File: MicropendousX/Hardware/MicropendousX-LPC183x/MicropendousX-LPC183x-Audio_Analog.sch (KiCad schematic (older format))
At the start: 9 parts, among them IC1 LPC183X, J1 DC_POWER_JACK, U9 OPENNECT-CONTROLLER-I2S_3V3-P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

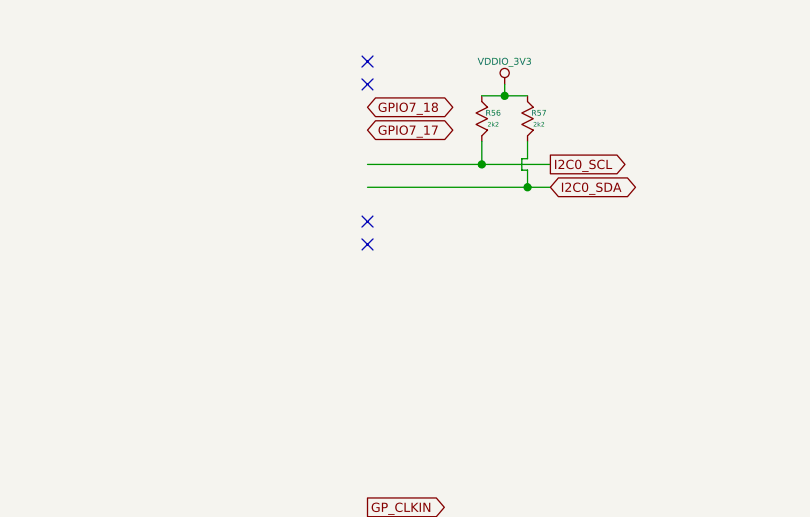
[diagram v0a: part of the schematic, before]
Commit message: Update unfinished LPC183x-based design.
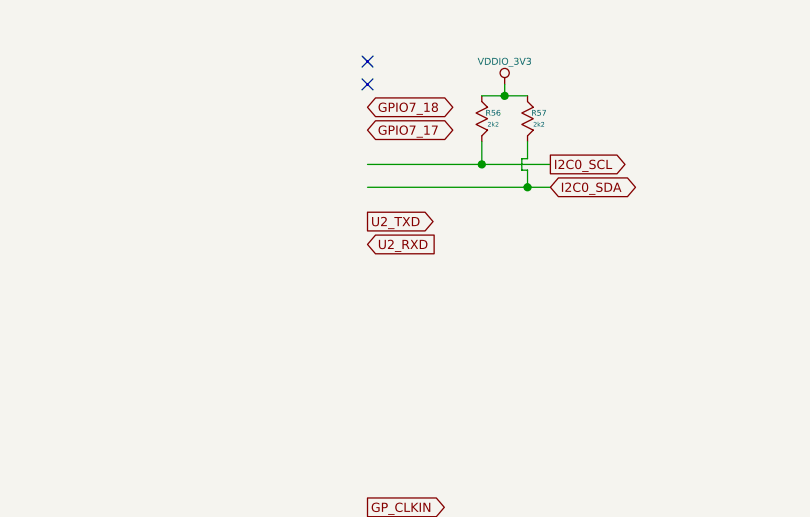
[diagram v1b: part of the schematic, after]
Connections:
- net labels added: U2_RXD, U2_TXD
- no-connect marks 18 -> 16
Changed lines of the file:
@@
-EESchema Schematic File Version 2  date 8/15/2011 4:26:38 PM
+EESchema Schematic File Version 2  date 8/20/2011 8:34:09 PM
 LIBS:power
 LIBS:device
@@
 $Descr A4 11700 8267
 encoding utf-8
-Sheet 3 7
+Sheet 5 9
 Title "MicropendousX-LPC183x"
-Date "15 aug 2011"
+Date "21 aug 2011"
 Rev "1.0"
 Comp "Opendous Inc."
@@
 Comment4 "www.MicropendousX.org"
 $EndDescr
+Text GLabel 4050 2100 2    40   Input ~ 0
+U2_RXD
+Text GLabel 4050 2000 2    40   Output ~ 0
+U2_TXD
 Text GLabel 4050 6700 2    40   BiDi ~ 0
 GPIO3_7
@@
 GPIO7_17
 NoConn ~ 4050 7300
-NoConn ~ 4050 2000
-NoConn ~ 4050 2100
 NoConn ~ 4050 1300
 NoConn ~ 4050 1400
@@
 $EndComp
 $Comp
-L GND #PWR02
+L GND #PWR032
 U 1 1 4E4904B8
 P 8450 1500
-F 0 "#PWR02" H 8450 1500 30  0001 C CNN
+F 0 "#PWR032" H 8450 1500 30  0001 C CNN
 F 1 "GND" H 8450 1430 30  0001 C CNN
 	1    8450 1500
@@
 $EndComp
 $Comp
-L DC_VIN #PWR03
+L DC_VIN #PWR033
 U 1 1 4E4904AE
 P 8450 1250
-F 0 "#PWR03" H 8450 1350 30  0001 C CNN
+F 0 "#PWR033" H 8450 1350 30  0001 C CNN
 F 1 "DC_VIN" V 8450 1425 30  0000 C CNN
 	1    8450 1250
@@
 NoConn ~ 4050 3750
 $Comp
-L VDDIO_3V3 #PWR04
+L VDDIO_3V3 #PWR034
 U 1 1 4E23BF70
 P 4650 1400
-F 0 "#PWR04" H 4650 1500 30  0001 C CNN
+F 0 "#PWR034" H 4650 1500 30  0001 C CNN
 F 1 "VDDIO_3V3" H 4650 1500 30  0000 C CNN
 	1    4650 1400
@@
 $EndComp
 $Comp
-L GND #PWR05
+L GND #PWR035
 U 1 1 4E22B69E
 P 8100 5150
-F 0 "#PWR05" H 8100 5150 30  0001 C CNN
+F 0 "#PWR035" H 8100 5150 30  0001 C CNN
 F 1 "GND" H 8100 5080 30  0001 C CNN
 	1    8100 5150
@@
 $EndComp
 $Comp
-L DC_VIN #PWR06
+L DC_VIN #PWR036
 U 1 1 4E22B675
 P 7800 4850
-F 0 "#PWR06" H 7800 4950 30  0001 C CNN
+F 0 "#PWR036" H 7800 4950 30  0001 C CNN
 F 1 "DC_VIN" H 7800 4950 30  0000 C CNN
 	1    7800 4850
@@
 $EndComp
 $Comp
-L 5V0 #PWR07
+L 5V0 #PWR037
 U 1 1 4E22B673
 P 8200 4850
-F 0 "#PWR07" H 8200 4950 30  0001 C CNN
+F 0 "#PWR037" H 8200 4950 30  0001 C CNN
 F 1 "5V0" H 8200 4950 30  0000 C CNN
 	1    8200 4850
@@
 $EndComp
 $Comp
-L VDD3V3 #PWR08
+L VDD3V3 #PWR038
 U 1 1 4E22B671
 P 8000 4850
-F 0 "#PWR08" H 8000 4950 30  0001 C CNN
+F 0 "#PWR038" H 8000 4950 30  0001 C CNN
 F 1 "VDD3V3" H 8000 4950 30  0000 C CNN
 	1    8000 4850
@@
 $EndComp
 $Comp
-L VDDIO_3V3 #PWR09
+L VDDIO_3V3 #PWR039
 U 1 1 4E22B670
 P 8400 4850
-F 0 "#PWR09" H 8400 4950 30  0001 C CNN
+F 0 "#PWR039" H 8400 4950 30  0001 C CNN
 F 1 "VDDIO_3V3" H 8400 4950 30  0000 C CNN
 	1    8400 4850
@@
 $EndComp
 $Comp
-L GND #PWR010
+L GND #PWR040
 U 1 1 4E22B627
 P 8100 4500
-F 0 "#PWR010" H 8100 4500 30  0001 C CNN
+F 0 "#PWR040" H 8100 4500 30  0001 C CNN
 F 1 "GND" H 8100 4430 30  0001 C CNN
 	1    8100 4500
@@
 GPIO3_7
 $Comp
-L VDDIO_3V3 #PWR011
+L VDDIO_3V3 #PWR041
 U 1 1 4E22B516
 P 7400 4050
-F 0 "#PWR011" H 7400 4150 30  0001 C CNN
+F 0 "#PWR041" H 7400 4150 30  0001 C CNN
 F 1 "VDDIO_3V3" V 7400 4250 30  0000 C CNN
 	1    7400 4050
@@
 $EndComp
 $Comp
-L VDD3V3 #PWR012
+L VDD3V3 #PWR042
 U 1 1 4E22B4E3
 P 7400 2450
-F 0 "#PWR012" H 7400 2550 30  0001 C CNN
+F 0 "#PWR042" H 7400 2550 30  0001 C CNN
 F 1 "VDD3V3" V 7400 2625 30  0000 C CNN
 	1    7400 2450
@@
 $EndComp
 $Comp
-L 5V0 #PWR013
+L 5V0 #PWR043
 U 1 1 4E22B4D4
 P 7400 2550
-F 0 "#PWR013" H 7400 2650 30  0001 C CNN
+F 0 "#PWR043" H 7400 2650 30  0001 C CNN
 F 1 "5V0" V 7400 2675 30  0000 C CNN
 	1    7400 2550
@@
 $EndComp
 $Comp
-L DC_VIN #PWR014
+L DC_VIN #PWR044
 U 1 1 4E22B4C5
 P 8800 2500
-F 0 "#PWR014" H 8800 2600 30  0001 C CNN
+F 0 "#PWR044" H 8800 2600 30  0001 C CNN
 F 1 "DC_VIN" V 8800 2675 30  0000 C CNN
 	1    8800 2500

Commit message: Updated LPC183x Hardware Design
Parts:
- removed U9: OPENNECT-CONTROLLER-I2S_3V3-PWR_8W, symbol OPENNECT-CONTROLLER-I2S-PWR
- added IC3: 74VHC157, symbol LOGIC-MUX_QUAD_2TO1
- added TP?: CLKIN, symbol CONN_1
- added U9: Opennect-Controller-SingleEnded-x4, symbol OPENNECT-CONTROLLER-SINGLEENDED-X4
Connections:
- net labels added: EMC_A00, EMC_A01, EMC_A02, EMC_A03, EMC_A04, EMC_A05, EMC_A06, EMC_A07, EMC_A08, EMC_A09, EMC_A10, EMC_A11, EMC_A12, EMC_A13-ENET_MDC, EMC_D00, EMC_D01, EMC_D02, EMC_D03, EMC_D04, EMC_D05, EMC_D06, EMC_D07, I2S1_RX_SCK-CLKOUT, SPIFI_SCK-I2S1_TX_SCK-CGU_OUT1, ~EMC_BLS0~, ~EMC_CAS~, ~EMC_CS0~, ~EMC_OE~, ~EMC_RAS~, ~EMC_WE~
- wire segments 42 -> 46
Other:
- note added: "Opennect-Controller-I2S_3V3-PWR_8W"
- note added: "RX_SCK"
- note added: "RX_SDA"
- note added: "RX_WS"
- note added: "TX_SCK"
- note added: "TX_SDA"
- note added: "TX_WS"
- moved on the sheet: C103, C104, C105, C106, J1
